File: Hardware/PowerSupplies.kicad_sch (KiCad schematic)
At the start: 56 parts

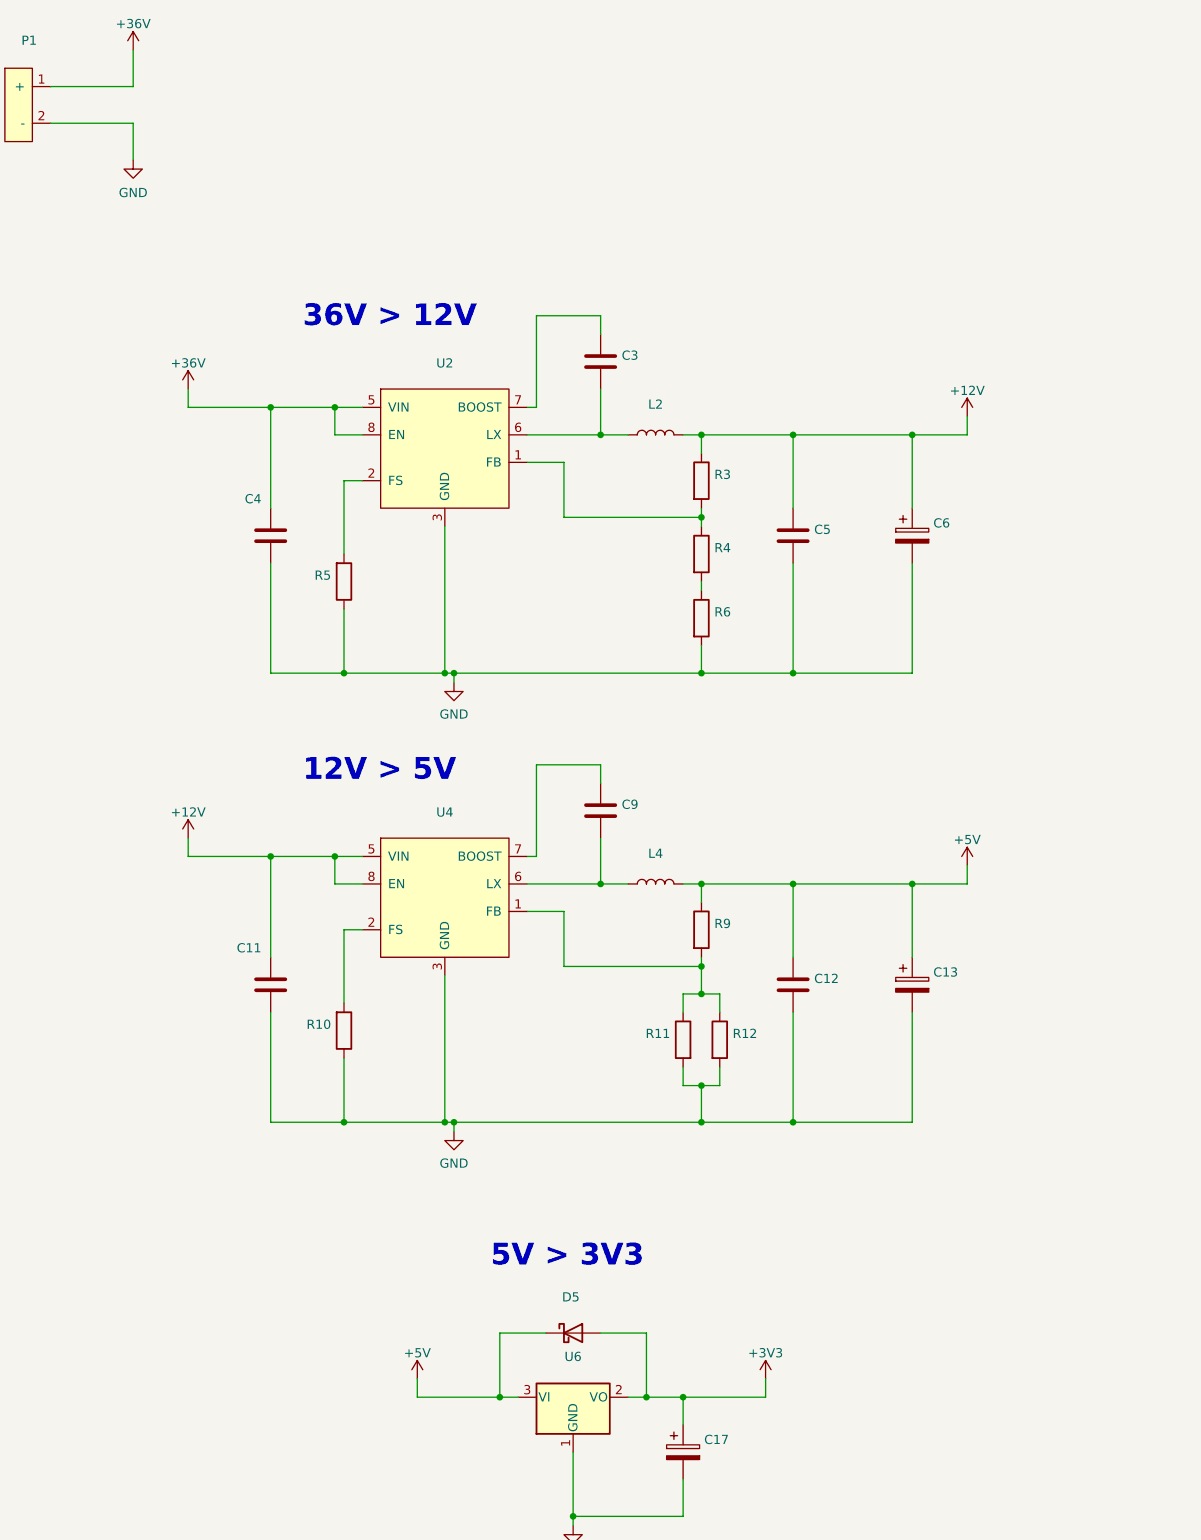
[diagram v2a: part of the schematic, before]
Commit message: Whoops, acidentally wiped all part assignments somehow. corrected.
Only pending footprint creation is for two switches.
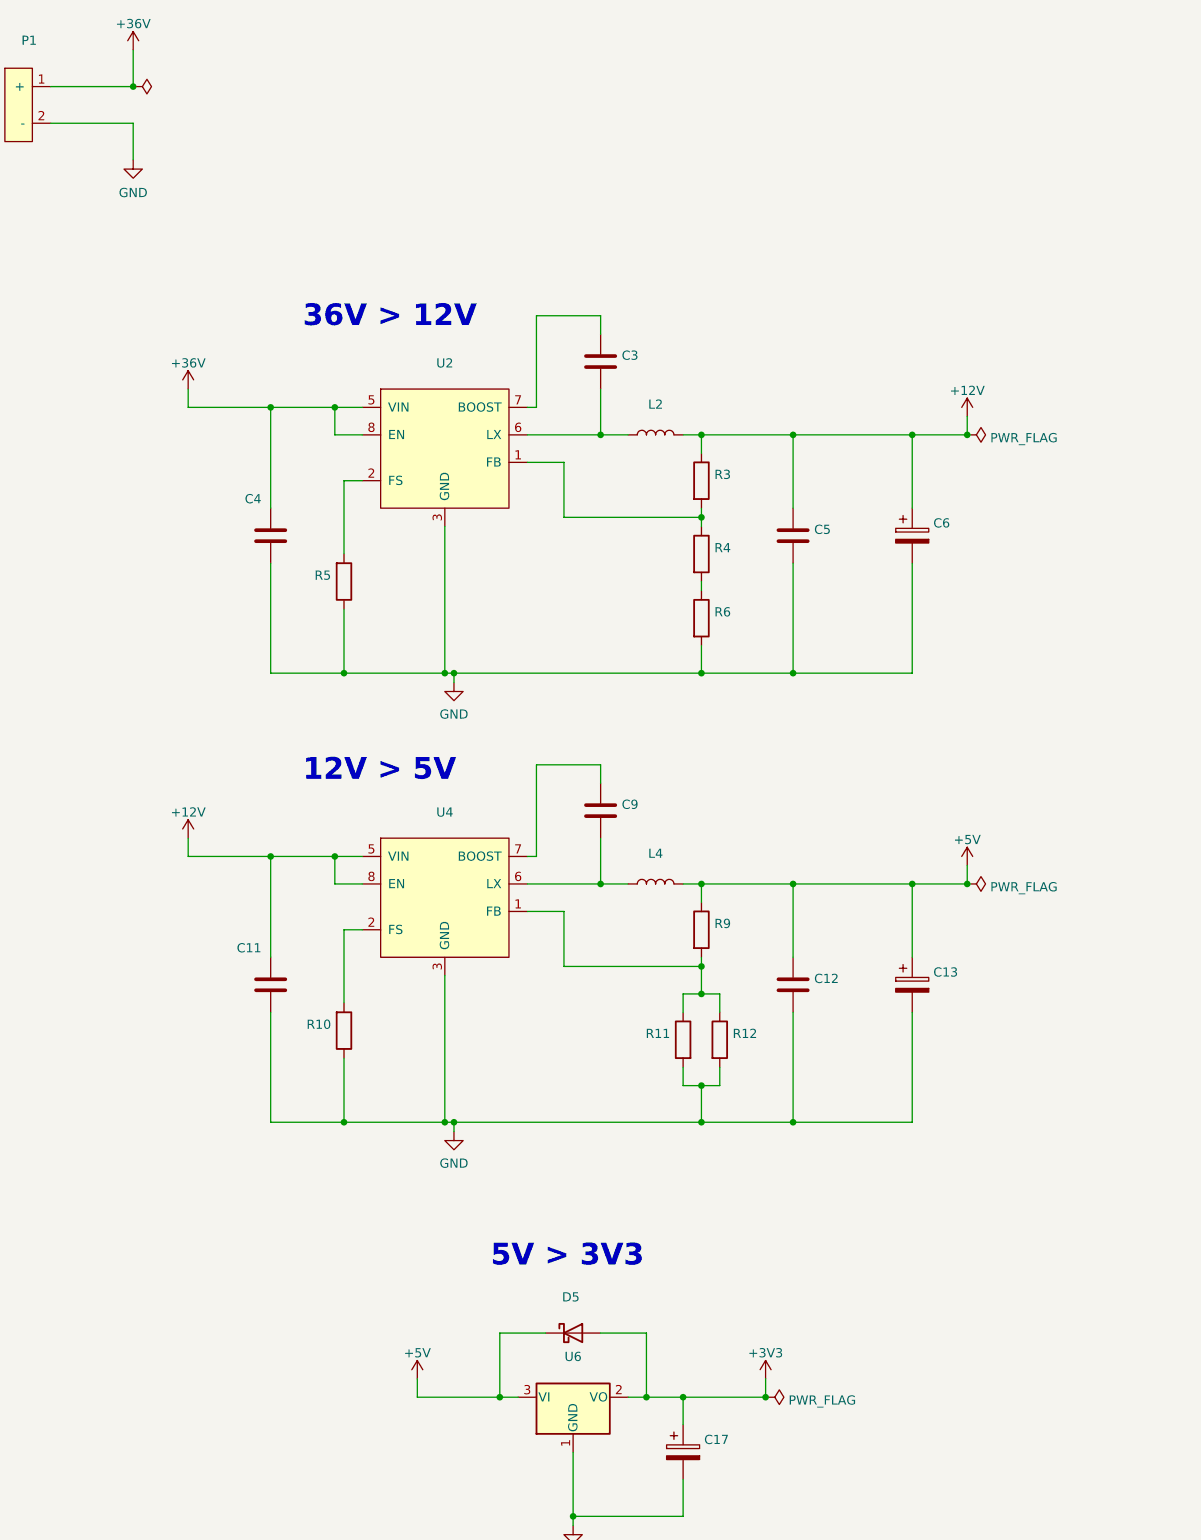
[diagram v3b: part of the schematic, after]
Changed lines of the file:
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@@
   (title_block
     (title "Sunrise Lamp LED driver")
-    (date "2022-04-23")
+    (date "2022-10-30")
     (rev "Mk1")
     (company "B E Searle")
@@
   (junction (at 119.38 143.51) (diameter 0) (color 0 0 0 0)
   )
+  (junction (at 54.61 33.02) (diameter 0) (color 0 0 0 0)
+  )
   (junction (at 83.82 176.53) (diameter 0) (color 0 0 0 0)
   )
@@
   (junction (at 331.47 88.9) (diameter 1.016) (color 0 0 0 0)
   )
+  (junction (at 142.24 214.63) (diameter 0) (color 0 0 0 0)
+  )
   (junction (at 345.44 88.9) (diameter 1.016) (color 0 0 0 0)
   )
+  (junction (at 170.18 81.28) (diameter 0) (color 0 0 0 0)
+  )
   (junction (at 133.35 92.71) (diameter 0) (color 0 0 0 0)
   )
@@
   )
   (junction (at 115.57 231.14) (diameter 0) (color 0 0 0 0)
+  )
+  (junction (at 170.18 143.51) (diameter 0) (color 0 0 0 0)
   )
   (junction (at 146.05 81.28) (diameter 0) (color 0 0 0 0)
@@
     (pin "1")
     (pin "2")
+  )
+  (symbol (lib_id "power:PWR_FLAG") (at 54.61 33.02 270) (unit 1)
+    (in_bom yes) (on_board yes) (fields_autoplaced)
+    (property "Reference" "#FLG0102" (id 0) (at 56.515 33.02 0)
+      (effects (font (size 1.27 1.27)) hide)
+    )
+    (property "Value" "" (id 1) (at 57.785 33.4538 90)
+      (effects (font (size 1.27 1.27)) (justify left))
+    )
+    (property "Footprint" "" (id 2) (at 54.61 33.02 0)
+      (effects (font (size 1.27 1.27)) hide)
+    )
+    (property "Datasheet" "~" (id 3) (at 54.61 33.02 0)
+      (effects (font (size 1.27 1.27)) hide)
+    )
+    (pin "1")
   )
   (symbol (lib_id "power:+36V") (at 54.61 27.94 0) (unit 1)
@@
     (pin "2")
   )
+  (symbol (lib_id "power:PWR_FLAG") (at 170.18 143.51 270) (unit 1)
+    (in_bom yes) (on_board yes) (fields_autoplaced)
+    (property "Reference" "#FLG0104" (id 0) (at 172.085 143.51 0)
+      (effects (font (size 1.27 1.27)) hide)
+    )
+    (property "Value" "PWR_FLAG" (id 1) (at 173.355 143.9438 90)
+      (effects (font (size 1.27 1.27)) (justify left))
+    )
+    (property "Footprint" "" (id 2) (at 170.18 143.51 0)
+      (effects (font (size 1.27 1.27)) hide)
+    )
+    (property "Datasheet" "~" (id 3) (at 170.18 143.51 0)
+      (effects (font (size 1.27 1.27)) hide)
+    )
+    (pin "1")
+  )
   (symbol (lib_id "Device:R") (at 133.35 106.68 0) (unit 1)
     (in_bom yes) (on_board yes)
@@
     (pin "1")
     (pin "2")
+  )
+  (symbol (lib_id "power:PWR_FLAG") (at 170.18 81.28 270) (unit 1)
+    (in_bom yes) (on_board yes) (fields_autoplaced)
+    (property "Reference" "#FLG0105" (id 0) (at 172.085 81.28 0)
+      (effects (font (size 1.27 1.27)) hide)
+    )
+    (property "Value" "PWR_FLAG" (id 1) (at 173.355 81.7138 90)
+      (effects (font (size 1.27 1.27)) (justify left))
+    )
+    (property "Footprint" "" (id 2) (at 170.18 81.28 0)
+      (effects (font (size 1.27 1.27)) hide)
+    )
+    (property "Datasheet" "~" (id 3) (at 170.18 81.28 0)
+      (effects (font (size 1.27 1.27)) hide)
+    )
+    (pin "1")
   )
   (symbol (lib_id "Device:C") (at 228.6 64.77 0) (unit 1)
@@
       (effects (font (size 1.27 1.27)) hide)
     )
+    (pin "1")
+  )
+  (symbol (lib_id "power:PWR_FLAG") (at 142.24 214.63 270) (unit 1)
+    (in_bom yes) (on_board yes) (fields_autoplaced)
+    (property "Reference" "#FLG0101" (id 0) (at 144.145 214.63 0)
+      (effects (font (size 1.27 1.27)) hide)
+    )
+    (property "Value" "PWR_FLAG" (id 1) (at 145.415 215.0638 90)
+      (effects (font (size 1.27 1.27)) (justify left))
+    )
+    (property "Footprint" "" (id 2) (at 142.24 214.63 0)
+      (effects (font (size 1.27 1.27)) hide)
+    )
+    (property "Datasheet" "~" (id 3) (at 142.24 214.63 0)
+      (effects (font (size 1.27 1.27)) hide)
+    )

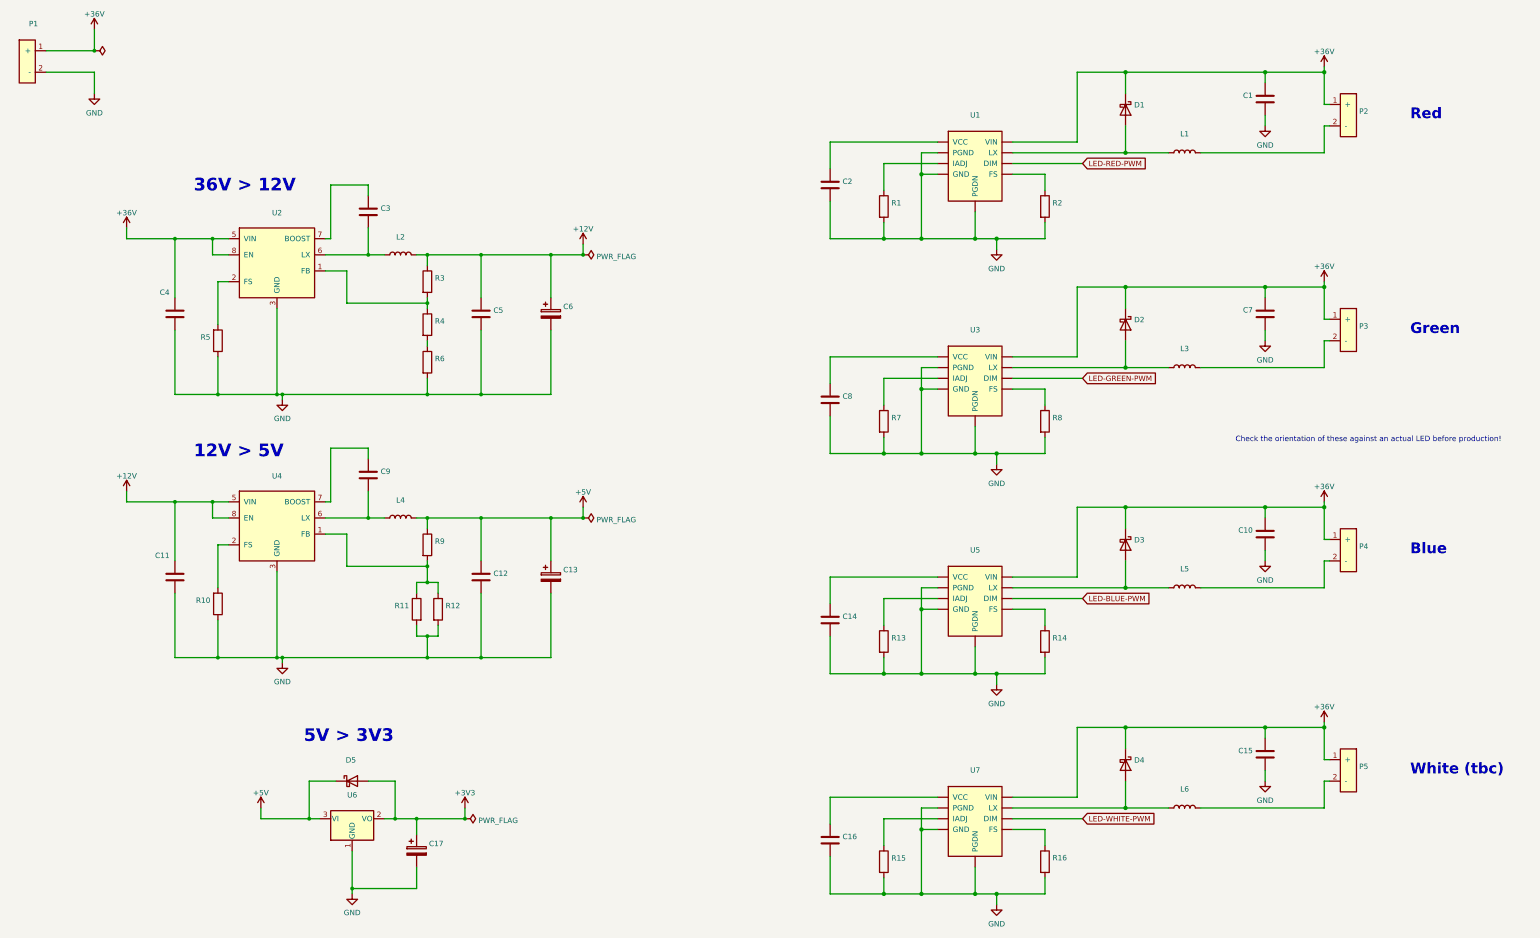
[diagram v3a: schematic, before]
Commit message: Layout changes
Changed XT60 outputs to Mini-Fit Jr., laid out 80mm fan edge cuts, started positioning conns
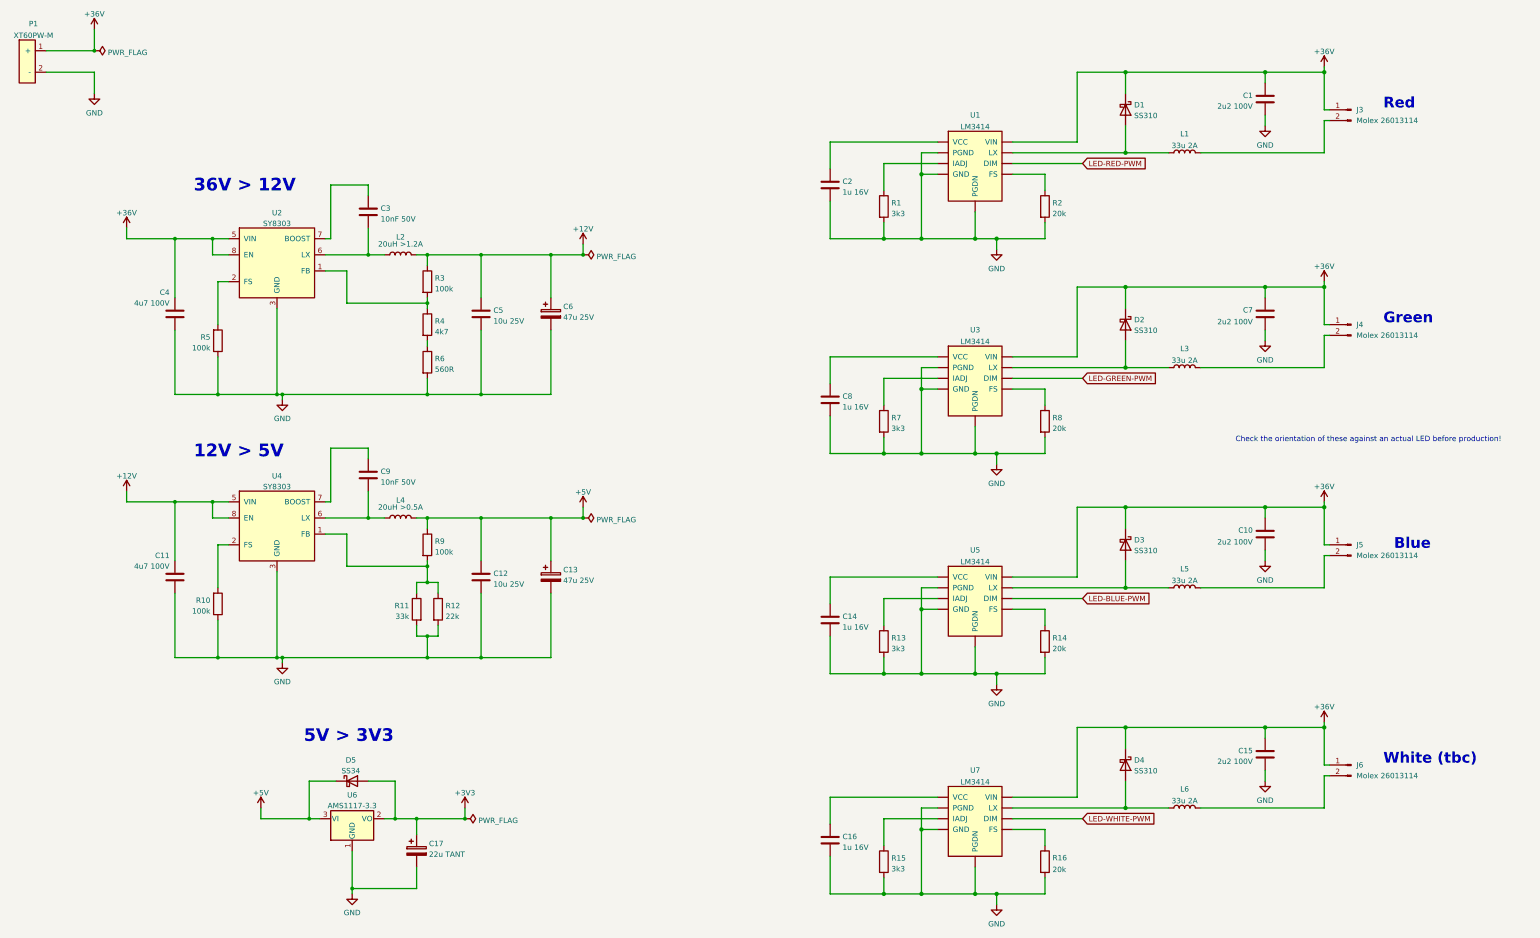
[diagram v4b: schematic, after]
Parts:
- removed P2, P3, P4, P5: (no value), symbol PersonalConnectors:XT60PW-F
- added J3, J4, J5, J6: Molex 26013114, Connector_Molex:Molex_Mini-Fit_Jr_5569-02A2_2x01_P4.20mm_Horizontal, symbol Connector:Conn_01x02_Male
- C1, C10, C15, C7: value (none) -> 2u2 100V; footprint (none) -> Capacitor_SMD:CP_Elec_6.3x5.4
- C11, C4: value (none) -> 4u7 100V; footprint (none) -> Capacitor_SMD:C_1210_3225Metric
- C12, C5: value (none) -> 10u 25V; footprint (none) -> Capacitor_SMD:C_0805_2012Metric_Pad1.18x1.45mm_HandSolder
- C13, C6: value (none) -> 47u 25V; footprint (none) -> Capacitor_SMD:CP_Elec_6.3x5.4
- C14, C16, C2, C8: value (none) -> 1u 16V; footprint (none) -> Capacitor_SMD:C_0805_2012Metric_Pad1.18x1.45mm_HandSolder
- C17: value (none) -> 22u TANT; footprint (none) -> Capacitor_Tantalum_SMD:CP_EIA-3528-15_AVX-H
- C3, C9: value (none) -> 10nF 50V; footprint (none) -> Capacitor_SMD:C_0805_2012Metric_Pad1.18x1.45mm_HandSolder
- D1, D2, D3, D4: value (none) -> SS310; footprint (none) -> Diode_SMD:D_SMA_Handsoldering
- D5: value (none) -> SS34; footprint (none) -> Diode_SMD:D_SMA_Handsoldering
- L1, L3, L5, L6: value (none) -> 33u 2A; footprint (none) -> Inductor_SMD:L_SigTra_SC3316F
- L2: value (none) -> 20uH >1.2A; footprint (none) -> Inductor_SMD:L_Taiyo-Yuden_NR-80xx
- L4: value (none) -> 20uH >0.5A; footprint (none) -> Inductor_SMD:L_Taiyo-Yuden_NR-80xx
- P1: value (none) -> XT60PW-M; footprint (none) -> PersonalConnectors:AMASS_XT60PW-M
- R1, R13, R15, R7: value (none) -> 3k3; footprint (none) -> Resistor_SMD:R_0603_1608Metric_Pad0.98x0.95mm_HandSolder
- R10, R3, R5, R9: value (none) -> 100k; footprint (none) -> Resistor_SMD:R_0603_1608Metric_Pad0.98x0.95mm_HandSolder
- R11: value (none) -> 33k; footprint (none) -> Resistor_SMD:R_0603_1608Metric_Pad0.98x0.95mm_HandSolder
- R12: value (none) -> 22k; footprint (none) -> Resistor_SMD:R_0603_1608Metric_Pad0.98x0.95mm_HandSolder
- R14, R16, R2, R8: value (none) -> 20k; footprint (none) -> Resistor_SMD:R_0603_1608Metric_Pad0.98x0.95mm_HandSolder
- R4: value (none) -> 4k7; footprint (none) -> Resistor_SMD:R_0603_1608Metric_Pad0.98x0.95mm_HandSolder
- R6: value (none) -> 560R; footprint (none) -> Resistor_SMD:R_0603_1608Metric_Pad0.98x0.95mm_HandSolder
- U1, U3, U5, U7: value (none) -> LM3414; footprint (none) -> PersonalDiscretes:TI_SO-PowerPAD-8_HandSolder
- U2, U4: value (none) -> SY8303; footprint (none) -> Package_TO_SOT_SMD:TSOT-23-8
- U6: value (none) -> AMS1117-3.3; footprint (none) -> Package_TO_SOT_SMD:SOT-223-3_TabPin2
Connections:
- net +36V: now also J3.1 (Pin_1), J4.1 (Pin_1), J5.1 (Pin_1), J6.1 (Pin_1)
- net at L1.2: now also J3.2 (Pin_2)
- net at L6.2: now also J6.2 (Pin_2)
- net at L5.2: now also J5.2 (Pin_2)
- net at L3.2: now also J4.2 (Pin_2)
